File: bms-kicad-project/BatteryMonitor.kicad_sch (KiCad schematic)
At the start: 5 parts, among them U1 LTC6804-2

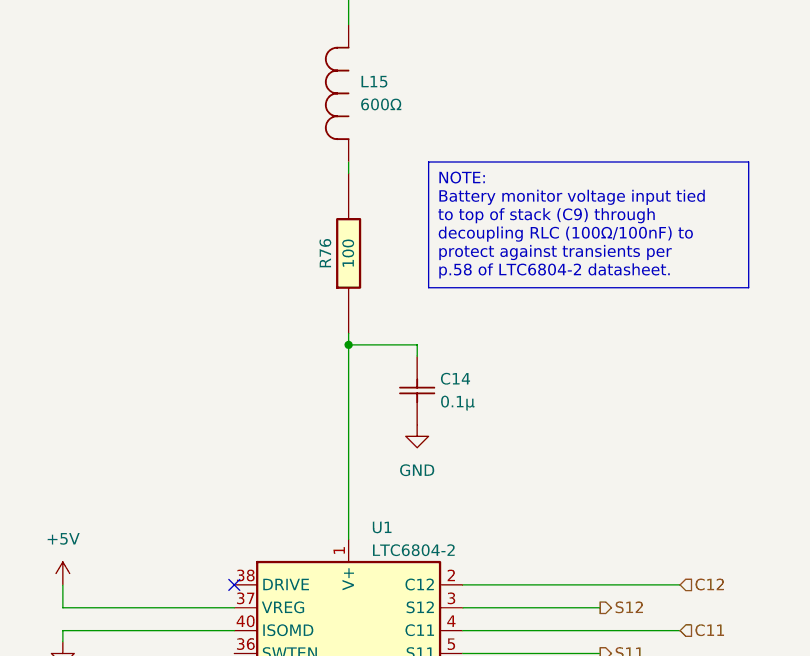
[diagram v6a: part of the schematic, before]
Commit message: feat: finished 5V reg circuit lgtm!
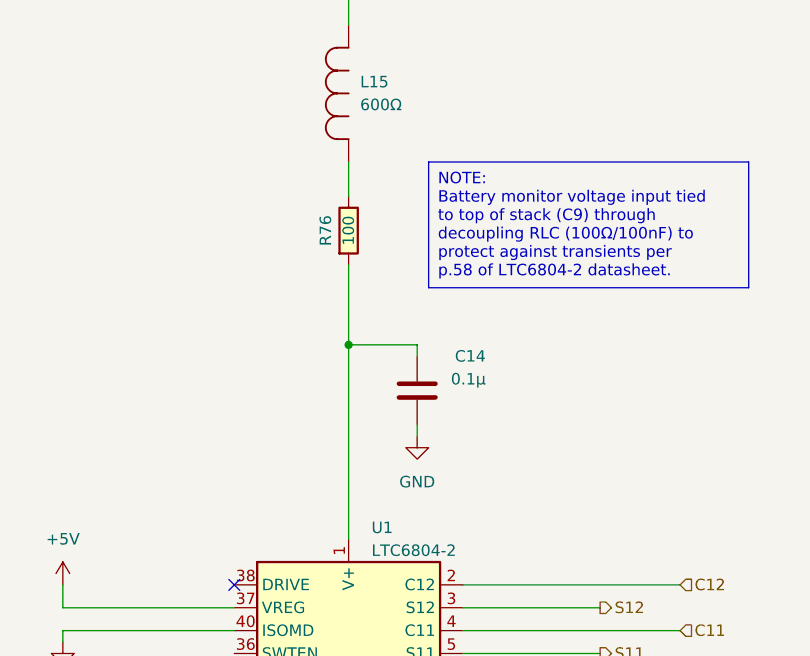
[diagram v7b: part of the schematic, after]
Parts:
- U1: Manufacturer Name (none) -> Analog Devices; Manufacturer Part Number (none) -> LTC6804-2; Mouser Part Number (none) -> 584-LTC6804IG-2#PBF; Mouser Price/Stock (none) -> https://www.mouser.com/ProductDetail/Analog-Devices/LTC6804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
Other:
- moved on the sheet: R76
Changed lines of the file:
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@@
     (stroke (width 0) (type default))
   )
-  (wire (pts (xy 193.04 49.53) (xy 193.04 50.8))
+  (wire (pts (xy 193.04 49.53) (xy 193.04 53.34))
     (stroke (width 0) (type default))
   )
@@
     (stroke (width 0) (type default))
   )
-  (wire (pts (xy 193.04 68.58) (xy 193.04 69.85))
+  (wire (pts (xy 193.04 60.96) (xy 193.04 69.85))
     (stroke (width 0) (type default))
   )
@@
   )
   (wire (pts (xy 161.29 135.89) (xy 161.29 142.24))
+    (stroke (width 0) (type default))
+  )
+  (wire (pts (xy 200.66 80.01) (xy 200.66 78.74))
     (stroke (width 0) (type default))
   )
@@
     (effects (font (size 1.27 1.27)) (justify left))
   )
-  (symbol (lib_id "FixedWing:CRCW0805100RFKEA") (at 193.04 68.58 90) (unit 1)
+  (symbol (lib_id "FixedWing:CRCW0805100RFKEA") (at 193.04 60.96 90) (unit 1)
     (in_bom yes) (on_board yes) (dnp no)
-    (property "Reference" "R76" (at 190.5 59.69 0)
-      (effects (font (size 1.27 1.27)))
-    )
-    (property "Value" "100" (at 193.04 59.69 0)
-      (effects (font (size 1.27 1.27)))
-    )
-    (property "Footprint" "RESC2012X50N" (at 289.23 54.61 0)
-      (effects (font (size 1.27 1.27)) (justify left top) hide)
-    )
-    (property "Datasheet" "http://www.vishay.com/docs/20035/dcrcwe3.pdf" (at 389.23 54.61 0)
-      (effects (font (size 1.27 1.27)) (justify left top) hide)
-    )
-    (property "Height" "0.5" (at 589.23 54.61 0)
-      (effects (font (size 1.27 1.27)) (justify left top) hide)
-    )
-    (property "Mouser Part Number" "71-CRCW0805-100-E3" (at 689.23 54.61 0)
-      (effects (font (size 1.27 1.27)) (justify left top) hide)
-    )
-    (property "Mouser Price/Stock" "https://www.mouser.co.uk/ProductDetail/Vishay-Dale/CRCW0805100RFKEA?qs=LOX6nxTstiYDPDKmuLyNLw%3D%3D" (at 789.23 54.61 0)
-      (effects (font (size 1.27 1.27)) (justify left top) hide)
-    )
-    (property "Manufacturer_Name" "Vishay" (at 889.23 54.61 0)
-      (effects (font (size 1.27 1.27)) (justify left top) hide)
-    )
-    (property "Manufacturer_Part_Number" "CRCW0805100RFKEA" (at 989.23 54.61 0)
+    (property "Reference" "R76" (at 190.5 57.15 0)
+      (effects (font (size 1.27 1.27)))
+    )
+    (property "Value" "100" (at 193.04 57.15 0)
+      (effects (font (size 1.27 1.27)))
+    )
+    (property "Footprint" "RESC2012X50N" (at 289.23 46.99 0)
+      (effects (font (size 1.27 1.27)) (justify left top) hide)
+    )
+    (property "Datasheet" "http://www.vishay.com/docs/20035/dcrcwe3.pdf" (at 389.23 46.99 0)
+      (effects (font (size 1.27 1.27)) (justify left top) hide)
+    )
+    (property "Height" "0.5" (at 589.23 46.99 0)
+      (effects (font (size 1.27 1.27)) (justify left top) hide)
+    )
+    (property "Mouser Part Number" "71-CRCW0805-100-E3" (at 689.23 46.99 0)
+      (effects (font (size 1.27 1.27)) (justify left top) hide)
+    )
+    (property "Mouser Price/Stock" "https://www.mouser.co.uk/ProductDetail/Vishay-Dale/CRCW0805100RFKEA?qs=LOX6nxTstiYDPDKmuLyNLw%3D%3D" (at 789.23 46.99 0)
+      (effects (font (size 1.27 1.27)) (justify left top) hide)
+    )
+    (property "Manufacturer_Name" "Vishay" (at 889.23 46.99 0)
+      (effects (font (size 1.27 1.27)) (justify left top) hide)
+    )
+    (property "Manufacturer_Part_Number" "CRCW0805100RFKEA" (at 989.23 46.99 0)
       (effects (font (size 1.27 1.27)) (justify left top) hide)
     )
@@
     )
     (property "Datasheet" "https://www.analog.com/media/en/technical-documentation/data-sheets/680412fc.pdf" (at 207.01 92.71 0)
+      (effects (font (size 1.27 1.27)) hide)
+    )
+    (property "Height" "~" (at 193.04 127 0)
+      (effects (font (size 1.27 1.27)) hide)
+    )
+    (property "Mouser Part Number" "584-LTC6804IG-2#PBF" (at 193.04 127 0)
+      (effects (font (size 1.27 1.27)) hide)
+    )
+    (property "Mouser Price/Stock" "https://www.mouser.com/ProductDetail/Analog-Devices/LTC6804IG-2PBF?qs=hVkxg5c3xu9J5aXeRrCrGw%3D%3D" (at 193.04 127 0)
+      (effects (font (size 1.27 1.27)) hide)
+    )
+    (property "Manufacturer Name" "Analog Devices" (at 193.04 127 0)
+      (effects (font (size 1.27 1.27)) hide)
+    )
+    (property "Manufacturer Part Number" "LTC6804-2" (at 193.04 127 0)
       (effects (font (size 1.27 1.27)) hide)
     )
@@
     )
   )
-  (symbol (lib_id "FixedWing:GCJ188R72A104KA01D") (at 200.66 74.93 180) (unit 1)
+  (symbol (lib_id "FixedWing:GCJ188R72A104KA01D") (at 200.66 71.12 270) (unit 1)
     (in_bom yes) (on_board yes) (dnp no)
-    (property "Reference" "C14" (at 203.2 73.66 0)
+    (property "Reference" "C14" (at 208.28 71.12 90)
       (effects (font (size 1.27 1.27)) (justify right))
     )
-    (property "Value" "0.1µ" (at 203.2 76.2 0)
+    (property "Value" "0.1µ" (at 208.28 73.66 90)
       (effects (font (size 1.27 1.27)) (justify right))
     )
-    (property "Footprint" "FixedWing:CAP_GCJ-18_MUR" (at 203.2 86.36 0)
+    (property "Footprint" "FixedWing:CAP_GCJ-18_MUR" (at 212.09 68.58 0)
       (effects (font (size 1.27 1.27) italic) hide)
     )
-    (property "Datasheet" "https://search.murata.co.jp/Ceramy/image/img/A01X/G101/ENG/GCJ21BR71A106KE01-01A.pdf" (at 203.2 86.36 0)
+    (property "Datasheet" "https://search.murata.co.jp/Ceramy/image/img/A01X/G101/ENG/GCJ21BR71A106KE01-01A.pdf" (at 212.09 68.58 0)
       (effects (font (size 1.27 1.27) italic) hide)
     )
-    (property "Manufacturer" "Murata Electronics" (at 201.93 86.36 0)
-      (effects (font (size 1.27 1.27)) hide)
-    )
-    (property "Manufacturer Part Number" "GCM21BR72A104KA37L" (at 200.66 74.93 0)
-      (effects (font (size 1.27 1.27)) hide)
-    )
-    (property "Manufacturer_Part_Number" "GCJ188R72A104KA01D" (at 203.2 86.36 0)
+    (property "Manufacturer" "Murata Electronics" (at 212.09 69.85 0)
+      (effects (font (size 1.27 1.27)) hide)
+    )
+    (property "Manufacturer Part Number" "GCM21BR72A104KA37L" (at 200.66 71.12 0)
+      (effects (font (size 1.27 1.27)) hide)
+    )
+    (property "Manufacturer_Part_Number" "GCJ188R72A104KA01D" (at 212.09 68.58 0)
       (effects (font (size 1.27 1.27)) hide)
     )
@@
     )
   )
-  (symbol (lib_id "power:GND") (at 200.66 78.74 0) (unit 1)
+  (symbol (lib_id "power:GND") (at 200.66 80.01 0) (unit 1)
     (in_bom yes) (on_board yes) (dnp no) (fields_autoplaced)
-    (property "Reference" "#PWR010" (at 200.66 85.09 0)
-      (effects (font (size 1.27 1.27)) hide)
-    )
-    (property "Value" "GND" (at 200.66 83.82 0)
-      (effects (font (size 1.27 1.27)))
-    )
-    (property "Footprint" "" (at 200.66 78.74 0)
-      (effects (font (size 1.27 1.27)) hide)
-    )
-    (property "Datasheet" "" (at 200.66 78.74 0)
-      (effects (font (size 1.27 1.27)) hide)
-    )
+    (property "Reference" "#PWR010" (at 200.66 86.36 0)
+      (effects (font (size 1.27 1.27)) hide)
+    )
+    (property "Value" "GND" (at 200.66 85.09 0)
+      (effects (font (size 1.27 1.27)))
+    )
+    (property "Footprint" "" (at 200.66 80.01 0)
+      (effects (font (size 1.27 1.27)) hide)
+    )
+    (property "Datasheet" "" (at 200.66 80.01 0)
+      (effects (font (size 1.27 1.27)) hide)
+    )

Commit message: Feature/current sensor (#17)
* feat: making sure my git still works

* feat: figured out battery stack monitor V+ biasing. Refer to task 5 on the punchlist for more details.

* feat: swapped out battery<->18V diode for cheaper alternative

* feat: started a new sheet for external connections and added current sensor

* feat: made a placeholder label to connect current sensor to LTC6811 GPIO

* feat: added remaining connectors to component library

* Wired up most external connections

* feat: Just shifting a few things around
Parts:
- removed C14: 0.1µ, FixedWing:CAP_GCJ-18_MUR, symbol FixedWing:GCJ188R72A104KA01D
- added C14, C15, C18, C19, C20: 4.7u, FixedWing:CAPC2012X145N, symbol FixedWing:GCM21BC71E475KE36L
- added C16, C17: 33n, FixedWing:CAPC2012X94N, symbol FixedWing:08053C333KAT2A
- added C21: 0.1µ, FixedWing:CAP_GCJ-18_MUR, symbol FixedWing:GCJ188R72A104KA01D
- added D1: B130LAW-7-F, FixedWing:SOD3716X145N, symbol FixedWing:B130LAW-7-F
- added D2, D3: 1N4448X-TP, FixedWing:1N4448XTP, symbol FixedWing:1N4448X-TP
- added K1: G6L-1P_DC5, FixedWing:RELAY_G6L-1P_DC5, symbol FixedWing:G6L-1P_DC5
- added L15: SDR0302-120ML, FixedWing:SDR0302-471KL, symbol FixedWing:SDR0302-120ML
- added Q13: BSS308PE_H6327, SOT95P260X110-3N, symbol FixedWing:BSS308PE_H6327
- added R75, R80: 56k2, FixedWing:RC0805N_YAG, symbol FixedWing:RC0805FR-0756K2L
- added R76, R78: 33k2, FixedWing:RC0805N_YAG, symbol FixedWing:RC0805FR-0733K2L
- added R77: 10k, FixedWing:KOA_Speer-RK73H2A-0-0-MFG, symbol FixedWing:RK73H2ATTD1002F
- added R79: 11k5, FixedWing:RC0805N_YAG, symbol FixedWing:RC0805FR-0711K5L
- added R81: 100k, FixedWing:RESC2012X60N, symbol FixedWing:RC0805FR-07100KL
- added U1: TPS61170DRVR, FixedWing:DRV6_1P6X1, symbol FixedWing:TPS61170DRVR
- added U2: SN74LVC1G17DCKR, FixedWing:DCK5, symbol FixedWing:SN74LVC1G17DCKR
- renumbered L15 to L16, R75 to R82, R76 to R83, U1 to U3
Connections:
- net +5V: now also Q13.2 (S), U2.5 (VCC)
- net +BATT: now also D2.2 (A), K1.2, R75.2; no longer L16.1
- net GND: now also C14.1, C15.1, C17.1, C18.1, C19.1, C20.1, C21.2, K1.5, R76.1, R77.1, R81.1, U1.3 (GND), U1.7 (EPAD), U2.3 (GND)
- net at R83.1, U3.1 (V+): now also C21.1
- net at L16.2: now also D2.1 (K), D3.1 (K); no longer R83.2
- net CUR_SENSE: now reaches U3.27 (GPIO1)
- new net: R78.1, U1.2 (COMP)
- new net: C16.2, R78.2
- new net: C18.2, C19.2, C20.2, D1.1 (K), D3.2 (A), R79.2
- new net: L16.1, R83.2
- new net: Q13.3 (D), R77.2, U2.2 (A)
- new net: C16.1, C17.2
- new net: R79.1, R80.2, U1.1 (FB)
- new net: D1.2 (A), L15.2, U1.4 (SW)
- new net: C14.2, C15.2, K1.4, L15.1, U1.5 (CTRL), U1.6 (VIN)
- new net: Q13.1 (G), R75.1, R76.2
- new net: R80.1, R81.2
- new net 4S_OR_LESS: K1.8, U2.4 (Y)
- no-connect marks 1 -> 2
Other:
- note added: "18V Step-Up Regulator"
- note added: "4S Battery Switching"
- note added: "LTC6811 Battery Stack Monitor"
- moved on the sheet: L16, R82, R83, U3
